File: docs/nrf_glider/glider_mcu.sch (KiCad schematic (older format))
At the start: 7 parts

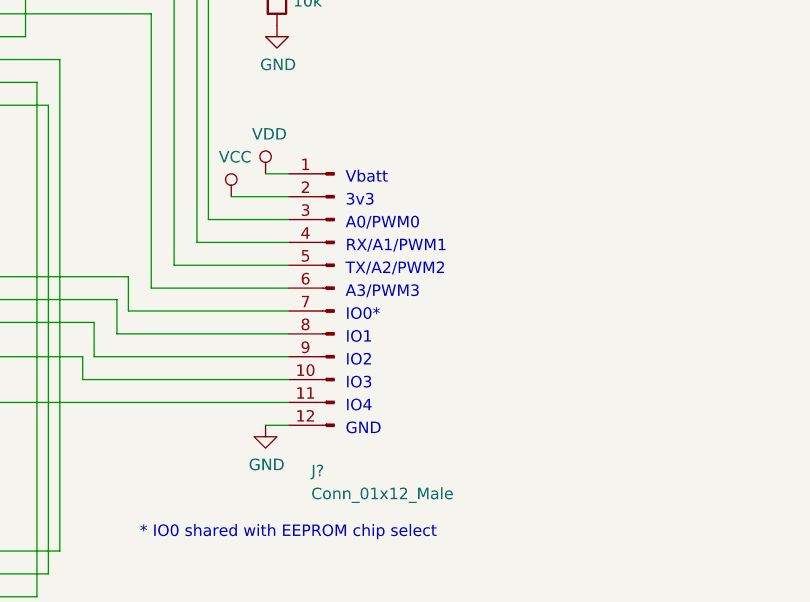
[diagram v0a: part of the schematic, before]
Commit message: added hierarchical sheets and labels
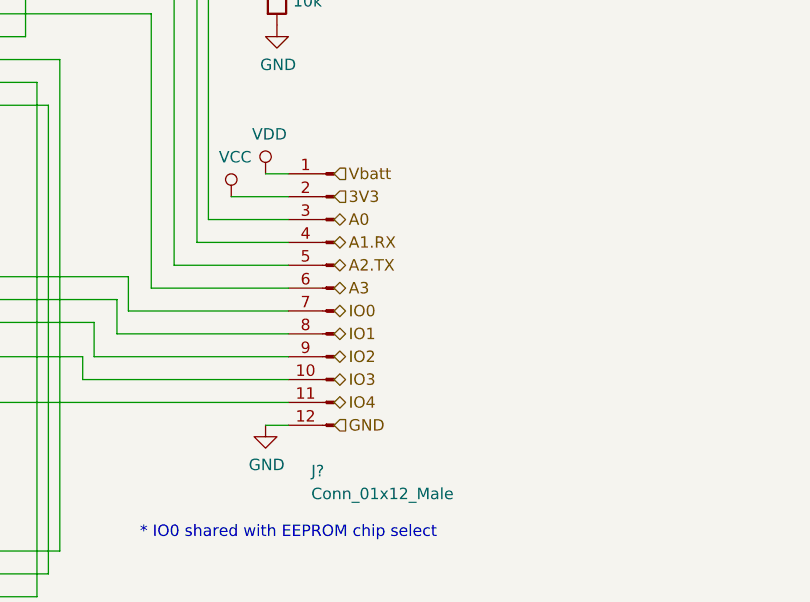
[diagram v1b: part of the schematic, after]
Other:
- note removed: "3v3"
- note removed: "A0/PWM0"
- note removed: "A3/PWM3"
- note removed: "IO0*"
- note removed: "IO1"
- note removed: "IO2"
- note removed: "IO3"
- note removed: "IO4"
- note removed: "RX/A1/PWM1"
- note removed: "TX/A2/PWM2"
- note removed: "Vbatt\n"
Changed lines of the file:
@@
 $Descr A4 11693 8268
 encoding utf-8
-Sheet 1 4
+Sheet 1 5
 Title ""
 Date ""
@@
 U 1 1 5BCECC43
 P 5350 2300
+AR Path="/5BD3906D/5BCECC43" Ref="U?"  Part="1"
+AR Path="/5BD39338/5BCECC43" Ref="U?"  Part="1"
 F 0 "U?" H 5828 2278 50  0000 L CNN
 F 1 "NRF24L01_Breakout" H 5828 2187 50  0000 L CNN
@@
 U 1 1 5BCECD91
 P 2850 3900
+AR Path="/5BD3906D/5BCECD91" Ref="U?"  Part="1"
+AR Path="/5BD39338/5BCECD91" Ref="U?"  Part="1"
 F 0 "U?" H 2850 4878 50  0000 C CNN
 F 1 "MSP430G2553IPW20" H 2850 4787 50  0000 C CNN
@@
 U 1 1 5BCED472
 P 3950 6250
+AR Path="/5BD3906D/5BCED472" Ref="U?"  Part="1"
+AR Path="/5BD39338/5BCED472" Ref="U?"  Part="1"
 F 0 "U?" H 3950 6728 50  0000 C CNN
 F 1 "25LC640" H 3950 6637 50  0000 C CNN
@@
 U 1 1 5BCEF2DA
 P 5350 1700
+AR Path="/5BD3906D/5BCEF2DA" Ref="#PWR?"  Part="1"
+AR Path="/5BD39338/5BCEF2DA" Ref="#PWR?"  Part="1"
 F 0 "#PWR?" H 5350 1550 50  0001 C CNN
 F 1 "VCC" H 5367 1873 50  0000 C CNN
@@
 U 1 1 5BCEF357
 P 5350 2900
+AR Path="/5BD3906D/5BCEF357" Ref="#PWR?"  Part="1"
+AR Path="/5BD39338/5BCEF357" Ref="#PWR?"  Part="1"
 F 0 "#PWR?" H 5350 2650 50  0001 C CNN
 F 1 "GND" H 5355 2727 50  0000 C CNN
@@
 U 1 1 5BCEF4A1
 P 3950 6550
+AR Path="/5BD3906D/5BCEF4A1" Ref="#PWR?"  Part="1"
+AR Path="/5BD39338/5BCEF4A1" Ref="#PWR?"  Part="1"
 F 0 "#PWR?" H 3950 6300 50  0001 C CNN
 F 1 "GND" H 3955 6377 50  0000 C CNN
@@
 U 1 1 5BCEF4DF
 P 2850 4650
+AR Path="/5BD3906D/5BCEF4DF" Ref="#PWR?"  Part="1"
+AR Path="/5BD39338/5BCEF4DF" Ref="#PWR?"  Part="1"
 F 0 "#PWR?" H 2850 4400 50  0001 C CNN
 F 1 "GND" H 2855 4477 50  0000 C CNN
@@
 U 1 1 5BCEF55C
 P 2200 3000
+AR Path="/5BD3906D/5BCEF55C" Ref="#PWR?"  Part="1"
+AR Path="/5BD39338/5BCEF55C" Ref="#PWR?"  Part="1"
 F 0 "#PWR?" H 2200 2850 50  0001 C CNN
 F 1 "VCC" H 2217 3173 50  0000 C CNN
@@
 U 1 1 5BCEF5D9
 P 4200 5950
+AR Path="/5BD3906D/5BCEF5D9" Ref="#PWR?"  Part="1"
+AR Path="/5BD39338/5BCEF5D9" Ref="#PWR?"  Part="1"
 F 0 "#PWR?" H 4200 5800 50  0001 C CNN
 F 1 "VCC" H 4217 6123 50  0000 C CNN
@@
 U 1 1 5BCF4A41
 P 6000 3400
+AR Path="/5BD3906D/5BCF4A41" Ref="R?"  Part="1"
+AR Path="/5BD39338/5BCF4A41" Ref="R?"  Part="1"
 F 0 "R?" H 6070 3446 50  0000 L CNN
 F 1 "20k" H 6070 3355 50  0000 L CNN
@@
 U 1 1 5BCF4AC6
 P 6000 3700
+AR Path="/5BD3906D/5BCF4AC6" Ref="R?"  Part="1"
+AR Path="/5BD39338/5BCF4AC6" Ref="R?"  Part="1"
 F 0 "R?" H 6070 3746 50  0000 L CNN
 F 1 "10k" H 6070 3655 50  0000 L CNN
@@
 U 1 1 5BCF4B6F
 P 6000 3850
+AR Path="/5BD3906D/5BCF4B6F" Ref="#PWR?"  Part="1"
+AR Path="/5BD39338/5BCF4B6F" Ref="#PWR?"  Part="1"
 F 0 "#PWR?" H 6000 3600 50  0001 C CNN
 F 1 "GND" H 6005 3677 50  0000 C CNN
@@
 U 1 1 5BCF63D1
 P 6000 3250
+AR Path="/5BD3906D/5BCF63D1" Ref="#PWR?"  Part="1"
+AR Path="/5BD39338/5BCF63D1" Ref="#PWR?"  Part="1"
 F 0 "#PWR?" H 6000 3100 50  0001 C CNN
 F 1 "VDD" H 6017 3423 50  0000 C CNN
@@
 U 1 1 5BCFA9FB
 P 6250 5000
+AR Path="/5BD3906D/5BCFA9FB" Ref="J?"  Part="1"
+AR Path="/5BD39338/5BCFA9FB" Ref="J?"  Part="1"
 F 0 "J?" H 6350 4200 50  0000 R CNN
 F 1 "Conn_01x12_Male" H 6350 4100 50  0000 R CNN
@@
 U 1 1 5BCFAD35
 P 5950 4500
+AR Path="/5BD3906D/5BCFAD35" Ref="#PWR?"  Part="1"
+AR Path="/5BD39338/5BCFAD35" Ref="#PWR?"  Part="1"
 F 0 "#PWR?" H 5950 4350 50  0001 C CNN
 F 1 "VDD" H 5967 4673 50  0000 C CNN
@@
 U 1 1 5BCFB594
 P 5800 4600
+AR Path="/5BD3906D/5BCFB594" Ref="#PWR?"  Part="1"
+AR Path="/5BD39338/5BCFB594" Ref="#PWR?"  Part="1"
 F 0 "#PWR?" H 5800 4450 50  0001 C CNN
 F 1 "VCC" H 5817 4773 50  0000 C CNN
@@
 U 1 1 5BCFBE51
 P 5950 5600
+AR Path="/5BD3906D/5BCFBE51" Ref="#PWR?"  Part="1"
+AR Path="/5BD39338/5BCFBE51" Ref="#PWR?"  Part="1"
 F 0 "#PWR?" H 5950 5350 50  0001 C CNN
 F 1 "GND" H 5955 5427 50  0000 C CNN
@@
 U 1 1 5BD41D4E
 P 6150 1050
+AR Path="/5BD3906D/5BD41D4E" Ref="J?"  Part="1"
+AR Path="/5BD39338/5BD41D4E" Ref="J?"  Part="1"
 F 0 "J?" H 6250 650 50  0000 R CNN
 F 1 "PROG" H 6250 550 50  0000 R CNN
@@
 U 1 1 5BD421B2
 P 5750 850
+AR Path="/5BD3906D/5BD421B2" Ref="#PWR?"  Part="1"
+AR Path="/5BD39338/5BD421B2" Ref="#PWR?"  Part="1"
 F 0 "#PWR?" H 5750 700 50  0001 C CNN
 F 1 "VCC" H 5767 1023 50  0000 C CNN
@@
 U 1 1 5BD44828
 P 5750 1350
+AR Path="/5BD3906D/5BD44828" Ref="#PWR?"  Part="1"
+AR Path="/5BD39338/5BD44828" Ref="#PWR?"  Part="1"
 F 0 "#PWR?" H 5750 1100 50  0001 C CNN
 F 1 "GND" H 5755 1177 50  0000 C CNN
@@
 Wire Wire Line
 	4800 3600 5650 3600
-Text Notes 6300 4550 0    50   ~ 0
-Vbatt\n
-Text Notes 6300 4650 0    50   ~ 0
-3v3
-Text Notes 6300 4750 0    50   ~ 0
-A0/PWM0
-Text Notes 6300 4850 0    50   ~ 0
-RX/A1/PWM1
-Text Notes 6300 4950 0    50   ~ 0
-TX/A2/PWM2
-Text Notes 6300 5050 0    50   ~ 0
-A3/PWM3
-Text Notes 6300 5150 0    50   ~ 0
-IO0*
-Text Notes 6300 5250 0    50   ~ 0
-IO1
-Text Notes 6300 5350 0    50   ~ 0
-IO2
-Text Notes 6300 5450 0    50   ~ 0
-IO3
-Text Notes 6300 5550 0    50   ~ 0
-IO4
 Text Notes 6200 900  0    50   ~ 0
 3V3
@@
 Text Notes 6200 1400 0    50   ~ 0
 GND
-Text Notes 6300 5650 0    50   ~ 0
-GND
 Wire Wire Line
 	3550 6350 1150 6350
@@
 Wire Wire Line
 	3950 5950 4200 5950
+Text HLabel 6250 4500 2    50   Input ~ 0
+Vbatt
+Text HLabel 6250 4600 2    50   Input ~ 0
+3V3
+Text HLabel 6250 4700 2    50   BiDi ~ 0
+A0
+Text HLabel 6250 4800 2    50   BiDi ~ 0
+A1.RX
+Text HLabel 6250 4900 2    50   BiDi ~ 0
+A2.TX
+Text HLabel 6250 5000 2    50   BiDi ~ 0
+A3
+Text HLabel 6250 5100 2    50   BiDi ~ 0
+IO0
+Text HLabel 6250 5200 2    50   BiDi ~ 0
+IO1
+Text HLabel 6250 5300 2    50   BiDi ~ 0
+IO2
+Text HLabel 6250 5400 2    50   BiDi ~ 0
+IO3
+Text HLabel 6250 5500 2    50   BiDi ~ 0
+IO4
+Text HLabel 6250 5600 2    50   Input ~ 0
+GND
 $EndSCHEMATC
